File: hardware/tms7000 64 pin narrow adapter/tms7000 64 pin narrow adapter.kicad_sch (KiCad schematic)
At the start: 2 parts, among them J1 plcc 68, U1 DIP40 male pins

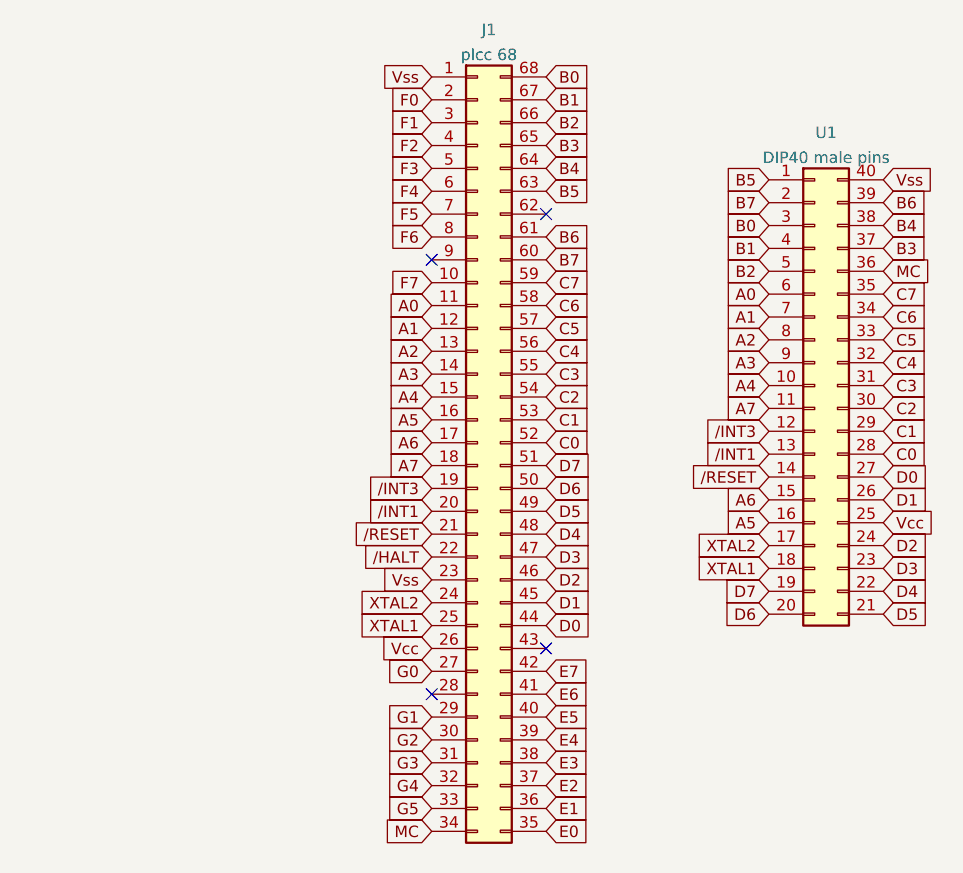
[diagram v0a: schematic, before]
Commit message: fixed plcc88, added qfp60, dip54, dip64, and dip64 small pitch
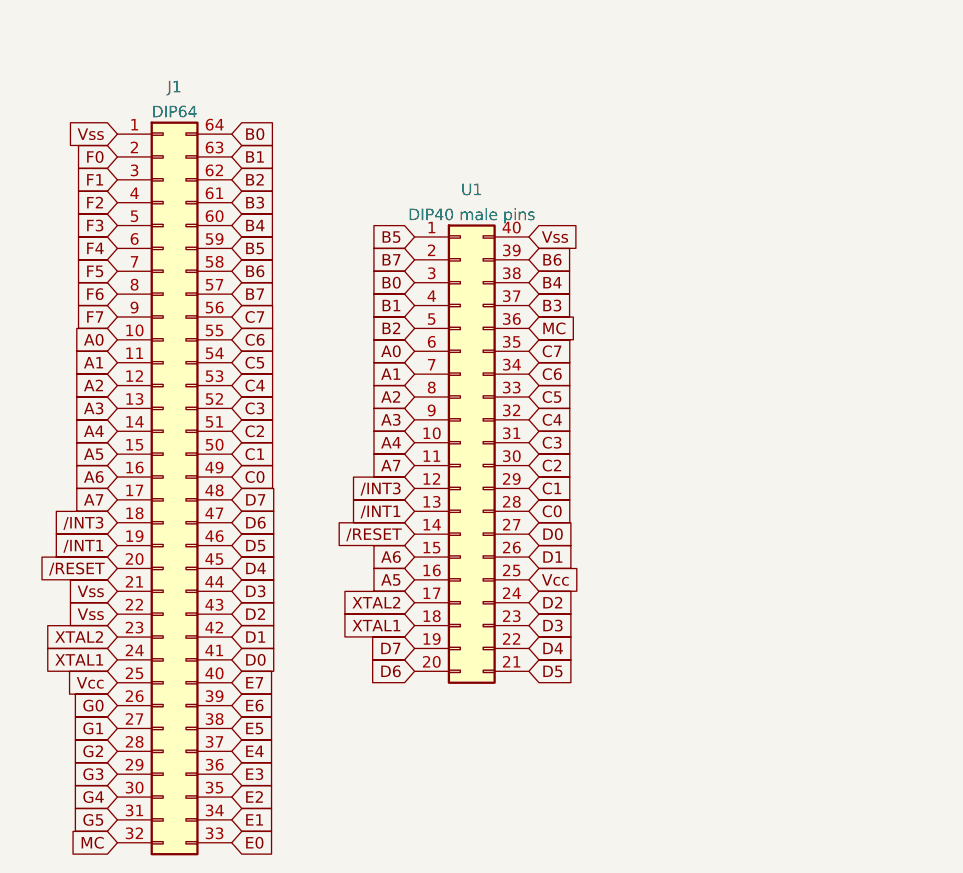
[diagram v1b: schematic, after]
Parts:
- removed J1: plcc 68, Package_LCC:PLCC-68_THT-Socket, symbol Connector_Generic:Conn_02x34_Counter_Clockwise
- added J1: DIP64, Evan's misc parts:DIP 64 1.78mm, symbol Connector_Generic:Conn_02x32_Counter_Clockwise
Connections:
- net A0: now also J1.10 (Pin_10)
- net A1: now also J1.11 (Pin_11)
- net A2: now also J1.12 (Pin_12)
- net A3: now also J1.13 (Pin_13)
- net A4: now also J1.14 (Pin_14)
- net A5: now also J1.15 (Pin_15)
- net A6: now also J1.16 (Pin_16)
- net A7: now also J1.17 (Pin_17)
- net B0: now also J1.64 (Pin_64)
- net B1: now also J1.63 (Pin_63)
- net B2: now also J1.62 (Pin_62)
- net B3: now also J1.61 (Pin_61)
- net B4: now also J1.60 (Pin_60)
- net B5: now also J1.59 (Pin_59)
- net B6: now also J1.58 (Pin_58)
- net B7: now also J1.57 (Pin_57)
- net C0: now also J1.49 (Pin_49)
- net C1: now also J1.50 (Pin_50)
- net C2: now also J1.51 (Pin_51)
- net C3: now also J1.52 (Pin_52)
- net C4: now also J1.53 (Pin_53)
- net C5: now also J1.54 (Pin_54)
- net C6: now also J1.55 (Pin_55)
- net C7: now also J1.56 (Pin_56)
- net D0: now also J1.41 (Pin_41)
- net D1: now also J1.42 (Pin_42)
- net D2: now also J1.43 (Pin_43)
- net D3: now also J1.44 (Pin_44)
- net D4: now also J1.45 (Pin_45)
- net D5: now also J1.46 (Pin_46)
- net D6: now also J1.47 (Pin_47)
- net D7: now also J1.48 (Pin_48)
- net E0: now also J1.33 (Pin_33)
- net E1: now also J1.34 (Pin_34)
- net E2: now also J1.35 (Pin_35)
- net E3: now also J1.36 (Pin_36)
- net E4: now also J1.37 (Pin_37)
- net E5: now also J1.38 (Pin_38)
- net E6: now also J1.39 (Pin_39)
- net E7: now also J1.40 (Pin_40)
- net F0: now also J1.2 (Pin_2)
- net F1: now also J1.3 (Pin_3)
- net F2: now also J1.4 (Pin_4)
- net F3: now also J1.5 (Pin_5)
- net F4: now also J1.6 (Pin_6)
- net F5: now also J1.7 (Pin_7)
- net F6: now also J1.8 (Pin_8)
- net F7: now also J1.9 (Pin_9)
- net G0: now also J1.26 (Pin_26)
- net G1: now also J1.27 (Pin_27)
- net G2: now also J1.28 (Pin_28)
- net G3: now also J1.29 (Pin_29)
- net G4: now also J1.30 (Pin_30)
- net G5: now also J1.31 (Pin_31)
- net MC: now also J1.32 (Pin_32)
- net Vcc: now also J1.25 (Pin_25)
- net Vss: now also J1.1 (Pin_1), J1.21 (Pin_21), J1.22 (Pin_22)
- net XTAL1: now also J1.24 (Pin_24)
- net XTAL2: now also J1.23 (Pin_23)
- net /INT1: now also J1.19 (Pin_19)
- net /INT3: now also J1.18 (Pin_18)
- net /RESET: now also J1.20 (Pin_20)
- no-connect marks 4 -> 0
